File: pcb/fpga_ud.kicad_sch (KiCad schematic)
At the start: 1 part

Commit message: fpga shite
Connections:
- net GND: now reaches U?.A1 (GND)
- net GND: now also U?.A11 (GND), U?.B8 (GND), U?.C15 (GND), U?.C5 (GND), U?.D12 (GND), U?.D2 (GND), U?.E9 (GND), U?.F10 (GND), U?.F16 (GND), U?.F6 (GND), U?.F8 (VCCBATT_0), U?.G13 (GND), U?.G3 (GND), U?.G7 (GNDADC_0), U?.G9 (GND), U?.H6 (GND), U?.J11 (GND), U?.J9 (GND), U?.K14 (GND), U?.K4 (GND), U?.K6 (GND), U?.L1 (GND), U?.L11 (GND), U?.M8 (GND), U?.N15 (GND), U?.N5 (GND), U?.P12 (GND), U?.P2 (GND), U?.R9 (GND), U?.T16 (GND), U?.T6 (GND)
- net +1V0: now reaches U?.E10 (VCCBRAM)
- net +1V0: now also U?.F11 (VCCBRAM), U?.F7 (VCCINT), U?.F9 (VCCINT), U?.G6 (VCCINT), U?.H9 (VCCINT), U?.J6 (VCCINT), U?.K9 (VCCINT), U?.L8 (VCCINT)
- net +1V8: now reaches U?.G10 (VCCAUX)
- net +1V8: now also U?.G8 (VCCADC_0), U?.J10 (VCCAUX), U?.K11 (VCCAUX), U?.L10 (VCCAUX)

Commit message: add footprints
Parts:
- U1301: renamed from U?; footprint (none) -> fpga:BGA256C100P16X16_1700X1700X155
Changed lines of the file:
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@@
   (symbol (lib_id "power:GND") (at 71.12 120.65 0) (unit 1)
     (in_bom yes) (on_board yes) (fields_autoplaced)
-    (property "Reference" "#PWR?" (id 0) (at 71.12 127 0)
+    (property "Reference" "#PWR01304" (id 0) (at 71.12 127 0)
       (effects (font (size 1.27 1.27)) hide)
     )
@@
   (symbol (lib_id "power:+1V0") (at 121.92 49.53 0) (unit 1)
     (in_bom yes) (on_board yes) (fields_autoplaced)
-    (property "Reference" "#PWR?" (id 0) (at 121.92 53.34 0)
+    (property "Reference" "#PWR01305" (id 0) (at 121.92 53.34 0)
       (effects (font (size 1.27 1.27)) hide)
     )
@@
   (symbol (lib_id "power:+1V8") (at 71.12 48.26 0) (unit 1)
     (in_bom yes) (on_board yes) (fields_autoplaced)
-    (property "Reference" "#PWR?" (id 0) (at 71.12 52.07 0)
+    (property "Reference" "#PWR01303" (id 0) (at 71.12 52.07 0)
       (effects (font (size 1.27 1.27)) hide)
     )
@@
   (symbol (lib_id "power:+1V8") (at 63.5 67.31 0) (unit 1)
     (in_bom yes) (on_board yes) (fields_autoplaced)
-    (property "Reference" "#PWR?" (id 0) (at 63.5 71.12 0)
+    (property "Reference" "#PWR01302" (id 0) (at 63.5 71.12 0)
       (effects (font (size 1.27 1.27)) hide)
     )
@@
   (symbol (lib_id "power:+1V0") (at 59.69 71.12 0) (unit 1)
     (in_bom yes) (on_board yes) (fields_autoplaced)
-    (property "Reference" "#PWR?" (id 0) (at 59.69 74.93 0)
+    (property "Reference" "#PWR01301" (id 0) (at 59.69 74.93 0)
       (effects (font (size 1.27 1.27)) hide)
     )
@@
   (symbol (lib_id "FPGA_Xilinx_Artix7:XC7A100T-FTG256") (at 96.52 85.09 0) (unit 4)
     (in_bom yes) (on_board yes) (fields_autoplaced)
-    (property "Reference" "U?" (id 0) (at 96.52 44.45 0))
+    (property "Reference" "U1301" (id 0) (at 96.52 44.45 0))
     (property "Value" "XC7A100T-FTG256" (id 1) (at 96.52 46.99 0))
-    (property "Footprint" "" (id 2) (at 96.52 85.09 0)
+    (property "Footprint" "fpga:BGA256C100P16X16_1700X1700X155" (id 2) (at 96.52 85.09 0)
       (effects (font (size 1.27 1.27)) hide)
     )
@@
   (symbol (lib_id "power:GND") (at 121.92 120.65 0) (unit 1)
     (in_bom yes) (on_board yes) (fields_autoplaced)
-    (property "Reference" "#PWR?" (id 0) (at 121.92 127 0)
-      (effects (font (size 1.27 1.27)) hide)
-    )
+    (property "Reference" "#PWR01306" (id 0) (at 121.92 127 0)
+      (effects (font (size 1.27 1.27)) hide)
+    )

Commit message: start layout
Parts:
- removed U1301: XC7A100T-FTG256, fpga:BGA256C100P16X16_1700X1700X155, symbol FPGA_Xilinx_Artix7:XC7A100T-FTG256
- added U666: XC7A75T-FTG256, Package_BGA:Xilinx_FTG256, symbol FPGA_Xilinx_Artix7:XC7A75T-FTG256
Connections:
- net +1V0: now also U666.A1 (GND), U666.A11 (GND), U666.B8 (GND), U666.C15 (GND), U666.C5 (GND), U666.D12 (GND), U666.D2 (GND), U666.E10 (VCCBRAM), U666.E9 (GND), U666.F10 (GND), U666.F11 (VCCBRAM), U666.F16 (GND), U666.F6 (GND), U666.F7 (VCCINT), U666.F8 (VCCBATT_0), U666.F9 (VCCINT), U666.G10 (VCCAUX), U666.G13 (GND), U666.G3 (GND), U666.G6 (VCCINT), U666.G7 (GNDADC_0), U666.G8 (VCCADC_0), U666.G9 (GND), U666.H6 (GND), U666.H9 (VCCINT), U666.J10 (VCCAUX), U666.J11 (GND), U666.J6 (VCCINT), U666.J9 (GND), U666.K11 (VCCAUX), U666.K14 (GND), U666.K4 (GND), U666.K6 (GND), U666.K9 (VCCINT), U666.L1 (GND), U666.L10 (VCCAUX), U666.L11 (GND), U666.L8 (VCCINT), U666.M8 (GND), U666.N15 (GND), U666.N5 (GND), U666.P12 (GND), U666.P2 (GND), U666.R9 (GND), U666.T16 (GND), U666.T6 (GND)

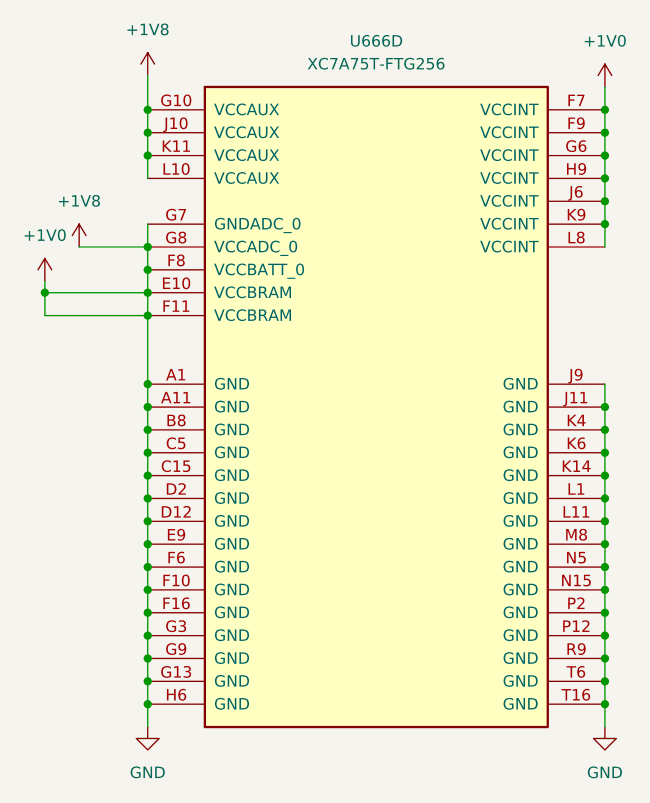
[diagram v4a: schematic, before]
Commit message: connect onboard controller
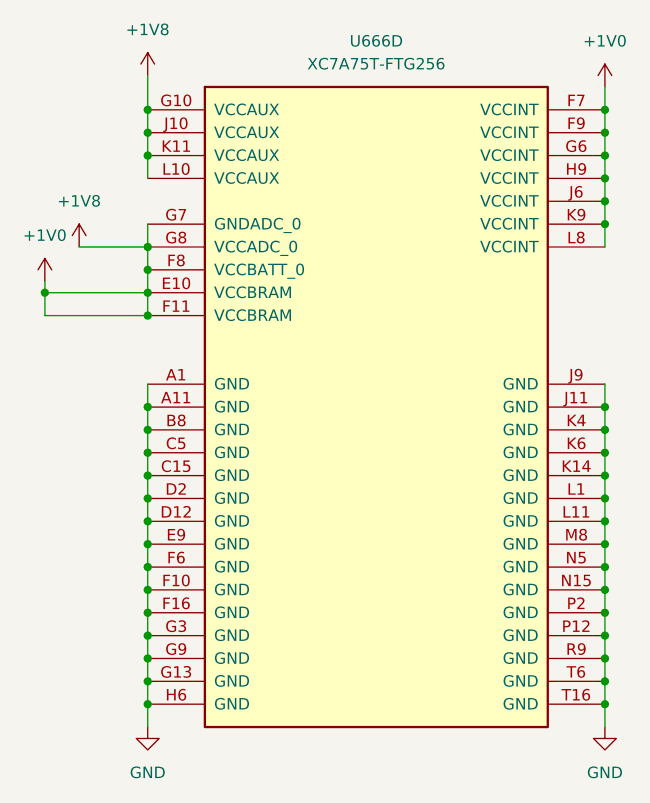
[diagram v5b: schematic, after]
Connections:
- net +1V0: no longer U666.A1 (GND), U666.A11 (GND), U666.B8 (GND), U666.C15 (GND), U666.C5 (GND), U666.D12 (GND), U666.D2 (GND), U666.E9 (GND), U666.F10 (GND), U666.F16 (GND), U666.F6 (GND), U666.G13 (GND), U666.G3 (GND), U666.G9 (GND), U666.H6 (GND), U666.J11 (GND), U666.J9 (GND), U666.K14 (GND), U666.K4 (GND), U666.K6 (GND), U666.L1 (GND), U666.L11 (GND), U666.M8 (GND), U666.N15 (GND), U666.N5 (GND), U666.P12 (GND), U666.P2 (GND), U666.R9 (GND), U666.T16 (GND), U666.T6 (GND)
- new net GND: U666.A1 (GND), U666.A11 (GND), U666.B8 (GND), U666.C15 (GND), U666.C5 (GND), U666.D12 (GND), U666.D2 (GND), U666.E9 (GND), U666.F10 (GND), U666.F16 (GND), U666.F6 (GND), U666.G13 (GND), U666.G3 (GND), U666.G9 (GND), U666.H6 (GND), U666.J11 (GND), U666.J9 (GND), U666.K14 (GND), U666.K4 (GND), U666.K6 (GND), U666.L1 (GND), U666.L11 (GND), U666.M8 (GND), U666.N15 (GND), U666.N5 (GND), U666.P12 (GND), U666.P2 (GND), U666.R9 (GND), U666.T16 (GND), U666.T6 (GND)
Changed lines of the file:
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@@
   (junction (at 121.92 105.41) (diameter 0) (color 0 0 0 0)
-  )
-  (junction (at 71.12 82.55) (diameter 0) (color 0 0 0 0)
   )
   (junction (at 71.12 95.25) (diameter 0) (color 0 0 0 0)
@@
     (stroke (width 0) (type default) (color 0 0 0 0))
   )
-  (wire (pts (xy 71.12 74.93) (xy 71.12 82.55))
-    (stroke (width 0) (type default) (color 0 0 0 0))
-  )

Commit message: fix nasty shorts
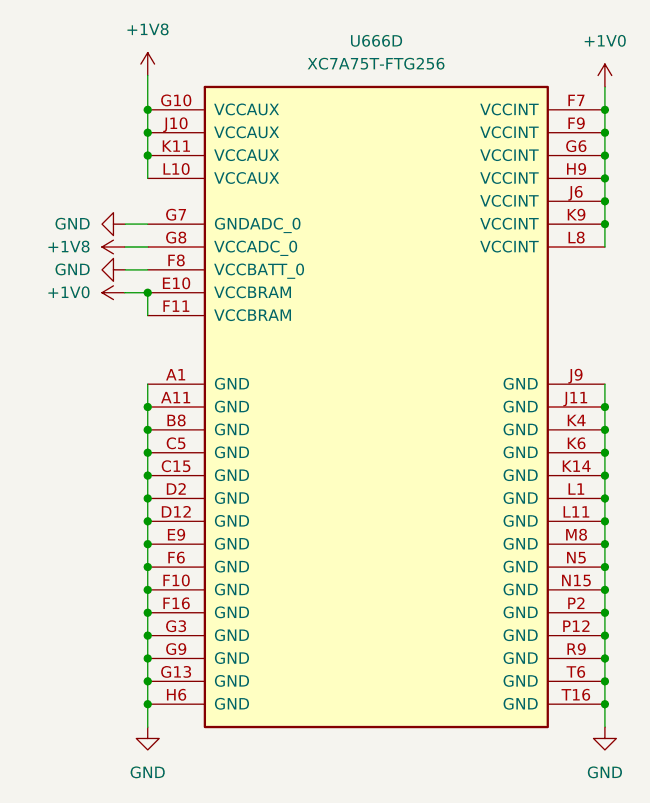
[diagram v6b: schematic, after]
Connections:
- net +1V0: no longer U666.F8 (VCCBATT_0), U666.G10 (VCCAUX), U666.G7 (GNDADC_0), U666.G8 (VCCADC_0), U666.J10 (VCCAUX), U666.K11 (VCCAUX), U666.L10 (VCCAUX)
- net GND: now also U666.F8 (VCCBATT_0), U666.G7 (GNDADC_0)
- new net +1V8: U666.G10 (VCCAUX), U666.G8 (VCCADC_0), U666.J10 (VCCAUX), U666.K11 (VCCAUX), U666.L10 (VCCAUX)
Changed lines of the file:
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@@
   (junction (at 121.92 95.25) (diameter 0) (color 0 0 0 0)
   )
-  (junction (at 71.12 74.93) (diameter 0) (color 0 0 0 0)
-  )
   (junction (at 71.12 85.09) (diameter 0) (color 0 0 0 0)
   )
@@
   (junction (at 121.92 107.95) (diameter 0) (color 0 0 0 0)
   )
-  (junction (at 59.69 72.39) (diameter 0) (color 0 0 0 0)
-  )
-  (junction (at 71.12 69.85) (diameter 0) (color 0 0 0 0)
-  )
   (junction (at 121.92 85.09) (diameter 0) (color 0 0 0 0)
   )
-  (junction (at 71.12 67.31) (diameter 0) (color 0 0 0 0)
-  )
   (junction (at 71.12 52.07) (diameter 0) (color 0 0 0 0)
   )
@@
   (junction (at 121.92 62.23) (diameter 0) (color 0 0 0 0)
   )
+  (junction (at 121.92 52.07) (diameter 0) (color 0 0 0 0)
+  )
+  (junction (at 71.12 87.63) (diameter 0) (color 0 0 0 0)
+  )
   (junction (at 71.12 72.39) (diameter 0) (color 0 0 0 0)
   )
-  (junction (at 121.92 52.07) (diameter 0) (color 0 0 0 0)
-  )
-  (junction (at 71.12 87.63) (diameter 0) (color 0 0 0 0)
-  )
   (junction (at 121.92 115.57) (diameter 0) (color 0 0 0 0)
   )
@@
     (stroke (width 0) (type default) (color 0 0 0 0))
   )
+  (wire (pts (xy 71.12 72.39) (xy 68.58 72.39))
+    (stroke (width 0) (type default) (color 0 0 0 0))
+  )
   (wire (pts (xy 121.92 105.41) (xy 121.92 107.95))
     (stroke (width 0) (type default) (color 0 0 0 0))
@@
     (stroke (width 0) (type default) (color 0 0 0 0))
   )
-  (wire (pts (xy 71.12 74.93) (xy 59.69 74.93))
-    (stroke (width 0) (type default) (color 0 0 0 0))
-  )
-  (wire (pts (xy 59.69 72.39) (xy 71.12 72.39))
-    (stroke (width 0) (type default) (color 0 0 0 0))
-  )
   (wire (pts (xy 71.12 48.26) (xy 71.12 52.07))
     (stroke (width 0) (type default) (color 0 0 0 0))
@@
     (stroke (width 0) (type default) (color 0 0 0 0))
   )
-  (wire (pts (xy 71.12 67.31) (xy 71.12 69.85))
-    (stroke (width 0) (type default) (color 0 0 0 0))
-  )
   (wire (pts (xy 71.12 57.15) (xy 71.12 59.69))
     (stroke (width 0) (type default) (color 0 0 0 0))
@@
     (stroke (width 0) (type default) (color 0 0 0 0))
   )
-  (wire (pts (xy 71.12 69.85) (xy 71.12 72.39))
-    (stroke (width 0) (type default) (color 0 0 0 0))
-  )
   (wire (pts (xy 71.12 90.17) (xy 71.12 92.71))
     (stroke (width 0) (type default) (color 0 0 0 0))
@@
     (stroke (width 0) (type default) (color 0 0 0 0))
   )
+  (wire (pts (xy 68.58 64.77) (xy 71.12 64.77))
+    (stroke (width 0) (type default) (color 0 0 0 0))
+  )
   (wire (pts (xy 71.12 92.71) (xy 71.12 95.25))
     (stroke (width 0) (type default) (color 0 0 0 0))
@@
     (stroke (width 0) (type default) (color 0 0 0 0))
   )
-  (wire (pts (xy 59.69 72.39) (xy 59.69 71.12))
-    (stroke (width 0) (type default) (color 0 0 0 0))
-  )
   (wire (pts (xy 121.92 107.95) (xy 121.92 110.49))
     (stroke (width 0) (type default) (color 0 0 0 0))
@@
     (stroke (width 0) (type default) (color 0 0 0 0))
   )
-  (wire (pts (xy 71.12 72.39) (xy 71.12 74.93))
-    (stroke (width 0) (type default) (color 0 0 0 0))
-  )
   (wire (pts (xy 121.92 90.17) (xy 121.92 92.71))
     (stroke (width 0) (type default) (color 0 0 0 0))
@@
     (stroke (width 0) (type default) (color 0 0 0 0))
   )
-  (wire (pts (xy 59.69 74.93) (xy 59.69 72.39))
+  (wire (pts (xy 68.58 69.85) (xy 71.12 69.85))
+    (stroke (width 0) (type default) (color 0 0 0 0))
+  )
+  (wire (pts (xy 71.12 74.93) (xy 71.12 72.39))
     (stroke (width 0) (type default) (color 0 0 0 0))
   )
@@
     (stroke (width 0) (type default) (color 0 0 0 0))
   )
-  (wire (pts (xy 71.12 64.77) (xy 71.12 67.31))
-    (stroke (width 0) (type default) (color 0 0 0 0))
-  )
   (wire (pts (xy 71.12 95.25) (xy 71.12 97.79))
     (stroke (width 0) (type default) (color 0 0 0 0))
@@
     (stroke (width 0) (type default) (color 0 0 0 0))
   )
-  (wire (pts (xy 63.5 67.31) (xy 71.12 67.31))
+  (wire (pts (xy 68.58 67.31) (xy 71.12 67.31))
     (stroke (width 0) (type default) (color 0 0 0 0))
   )
   (wire (pts (xy 71.12 102.87) (xy 71.12 105.41))
     (stroke (width 0) (type default) (color 0 0 0 0))
+  )
+  (symbol (lib_id "power:GND") (at 68.58 64.77 270) (unit 1)
+    (in_bom yes) (on_board yes) (fields_autoplaced)
+    (property "Reference" "#PWR?" (id 0) (at 62.23 64.77 0)
+      (effects (font (size 1.27 1.27)) hide)
+    )
+    (property "Value" "GND" (id 1) (at 64.77 64.7699 90)
+      (effects (font (size 1.27 1.27)) (justify right))
+    )
+    (property "Footprint" "" (id 2) (at 68.58 64.77 0)
+      (effects (font (size 1.27 1.27)) hide)
+    )
+    (property "Datasheet" "" (id 3) (at 68.58 64.77 0)
+      (effects (font (size 1.27 1.27)) hide)
+    )
+    (pin "1")
   )
   (symbol (lib_id "power:GND") (at 71.12 120.65 0) (unit 1)
@@
     (pin "1")
   )
-  (symbol (lib_id "power:+1V8") (at 63.5 67.31 0) (unit 1)
-    (in_bom yes) (on_board yes) (fields_autoplaced)
-    (property "Reference" "#PWR01302" (id 0) (at 63.5 71.12 0)
-      (effects (font (size 1.27 1.27)) hide)
-    )
-    (property "Value" "+1V8" (id 1) (at 63.5 62.23 0))
-    (property "Footprint" "" (id 2) (at 63.5 67.31 0)
-      (effects (font (size 1.27 1.27)) hide)
-    )
-    (property "Datasheet" "" (id 3) (at 63.5 67.31 0)
+  (symbol (lib_id "power:+1V8") (at 68.58 67.31 90) (unit 1)
+    (in_bom yes) (on_board yes) (fields_autoplaced)
+    (property "Reference" "#PWR01302" (id 0) (at 72.39 67.31 0)
+      (effects (font (size 1.27 1.27)) hide)
+    )
+    (property "Value" "+1V8" (id 1) (at 64.77 67.3099 90)
+      (effects (font (size 1.27 1.27)) (justify left))
+    )
+    (property "Footprint" "" (id 2) (at 68.58 67.31 0)
+      (effects (font (size 1.27 1.27)) hide)
+    )
+    (property "Datasheet" "" (id 3) (at 68.58 67.31 0)
       (effects (font (size 1.27 1.27)) hide)
     )
@@
     (pin "T6")
   )
-  (symbol (lib_id "power:+1V0") (at 59.69 71.12 0) (unit 1)
-    (in_bom yes) (on_board yes) (fields_autoplaced)
-    (property "Reference" "#PWR01301" (id 0) (at 59.69 74.93 0)
-      (effects (font (size 1.27 1.27)) hide)
-    )
-    (property "Value" "+1V0" (id 1) (at 59.69 66.04 0))
-    (property "Footprint" "" (id 2) (at 59.69 71.12 0)
-      (effects (font (size 1.27 1.27)) hide)
-    )
-    (property "Datasheet" "" (id 3) (at 59.69 71.12 0)
-      (effects (font (size 1.27 1.27)) hide)
-    )
+  (symbol (lib_id "power:GND") (at 68.58 69.85 270) (unit 1)
+    (in_bom yes) (on_board yes) (fields_autoplaced)
+    (property "Reference" "#PWR?" (id 0) (at 62.23 69.85 0)
+      (effects (font (size 1.27 1.27)) hide)
+    )
+    (property "Value" "GND" (id 1) (at 64.77 69.8499 90)
+      (effects (font (size 1.27 1.27)) (justify right))
+    )
+    (property "Footprint" "" (id 2) (at 68.58 69.85 0)
+      (effects (font (size 1.27 1.27)) hide)
+    )
+    (property "Datasheet" "" (id 3) (at 68.58 69.85 0)
+      (effects (font (size 1.27 1.27)) hide)
+    )
+    (pin "1")
+  )
+  (symbol (lib_id "power:+1V0") (at 68.58 72.39 90) (unit 1)
+    (in_bom yes) (on_board yes) (fields_autoplaced)
+    (property "Reference" "#PWR01301" (id 0) (at 72.39 72.39 0)
+      (effects (font (size 1.27 1.27)) hide)
+    )
+    (property "Value" "+1V0" (id 1) (at 64.77 72.3899 90)
+      (effects (font (size 1.27 1.27)) (justify left))
+    )
+    (property "Footprint" "" (id 2) (at 68.58 72.39 0)
+      (effects (font (size 1.27 1.27)) hide)
+    )
+    (property "Datasheet" "" (id 3) (at 68.58 72.39 0)
+      (effects (font (size 1.27 1.27)) hide)
+    )

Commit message: fuckeru
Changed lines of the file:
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@@
   (symbol (lib_id "power:GND") (at 68.58 64.77 270) (unit 1)
     (in_bom yes) (on_board yes) (fields_autoplaced)
-    (property "Reference" "#PWR?" (id 0) (at 62.23 64.77 0)
-      (effects (font (size 1.27 1.27)) hide)
-    )
-    (property "Value" "GND" (id 1) (at 64.77 64.7699 90)
+    (property "Reference" "#PWR0110" (id 0) (at 62.23 64.77 0)
+      (effects (font (size 1.27 1.27)) hide)
+    )
+    (property "Value" "" (id 1) (at 64.77 64.7699 90)
       (effects (font (size 1.27 1.27)) (justify right))
     )
@@
   (symbol (lib_id "power:GND") (at 68.58 69.85 270) (unit 1)
     (in_bom yes) (on_board yes) (fields_autoplaced)
-    (property "Reference" "#PWR?" (id 0) (at 62.23 69.85 0)
-      (effects (font (size 1.27 1.27)) hide)
-    )
-    (property "Value" "GND" (id 1) (at 64.77 69.8499 90)
+    (property "Reference" "#PWR0109" (id 0) (at 62.23 69.85 0)
+      (effects (font (size 1.27 1.27)) hide)
+    )
+    (property "Value" "" (id 1) (at 64.77 69.8499 90)
       (effects (font (size 1.27 1.27)) (justify right))
     )

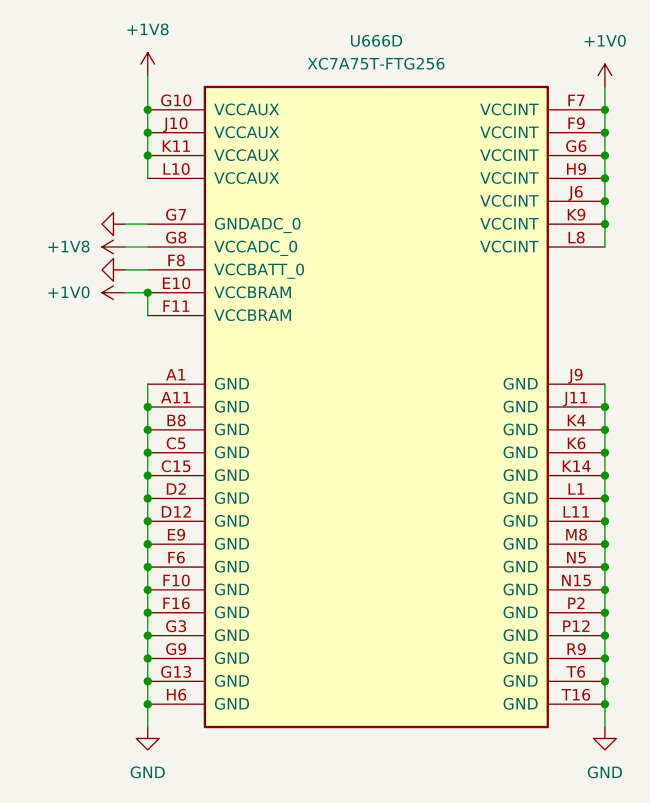
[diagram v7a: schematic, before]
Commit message: change footprint of debug_connector
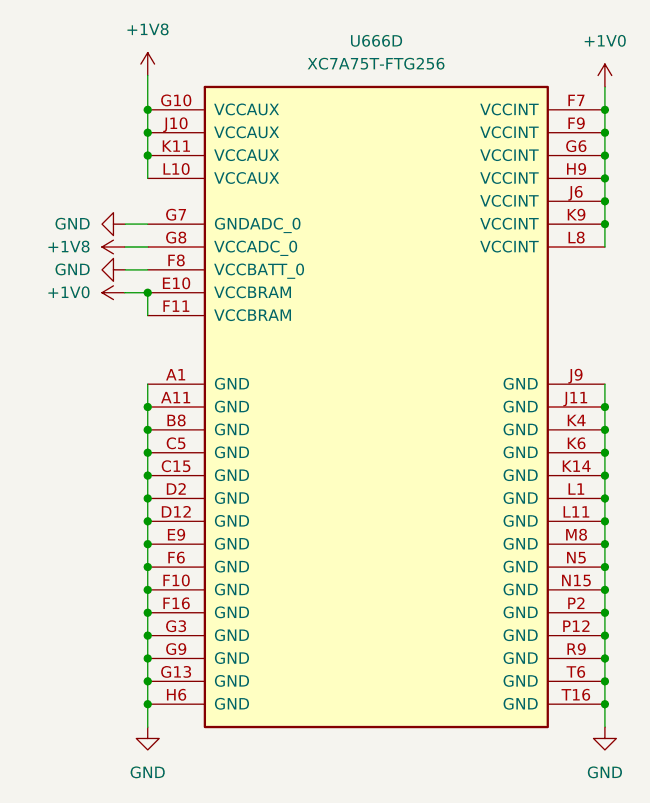
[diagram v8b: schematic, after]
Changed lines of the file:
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@@
       (effects (font (size 1.27 1.27)) hide)
     )
-    (property "Value" "" (id 1) (at 64.77 64.7699 90)
+    (property "Value" "GND" (id 1) (at 64.77 64.7699 90)
       (effects (font (size 1.27 1.27)) (justify right))
     )
@@
       (effects (font (size 1.27 1.27)) hide)
     )
-    (property "Value" "" (id 1) (at 64.77 69.8499 90)
+    (property "Value" "GND" (id 1) (at 64.77 69.8499 90)
       (effects (font (size 1.27 1.27)) (justify right))
     )
